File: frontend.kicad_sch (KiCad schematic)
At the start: 68 parts, among them P4 SMA, Q1 NMOS/PMOS, U12 BGS13SN8, U13 74LVC1G86, U14 BGS13SN8, U24 AP22652, U25 TRF37C73, U40 BGB741L7ESD

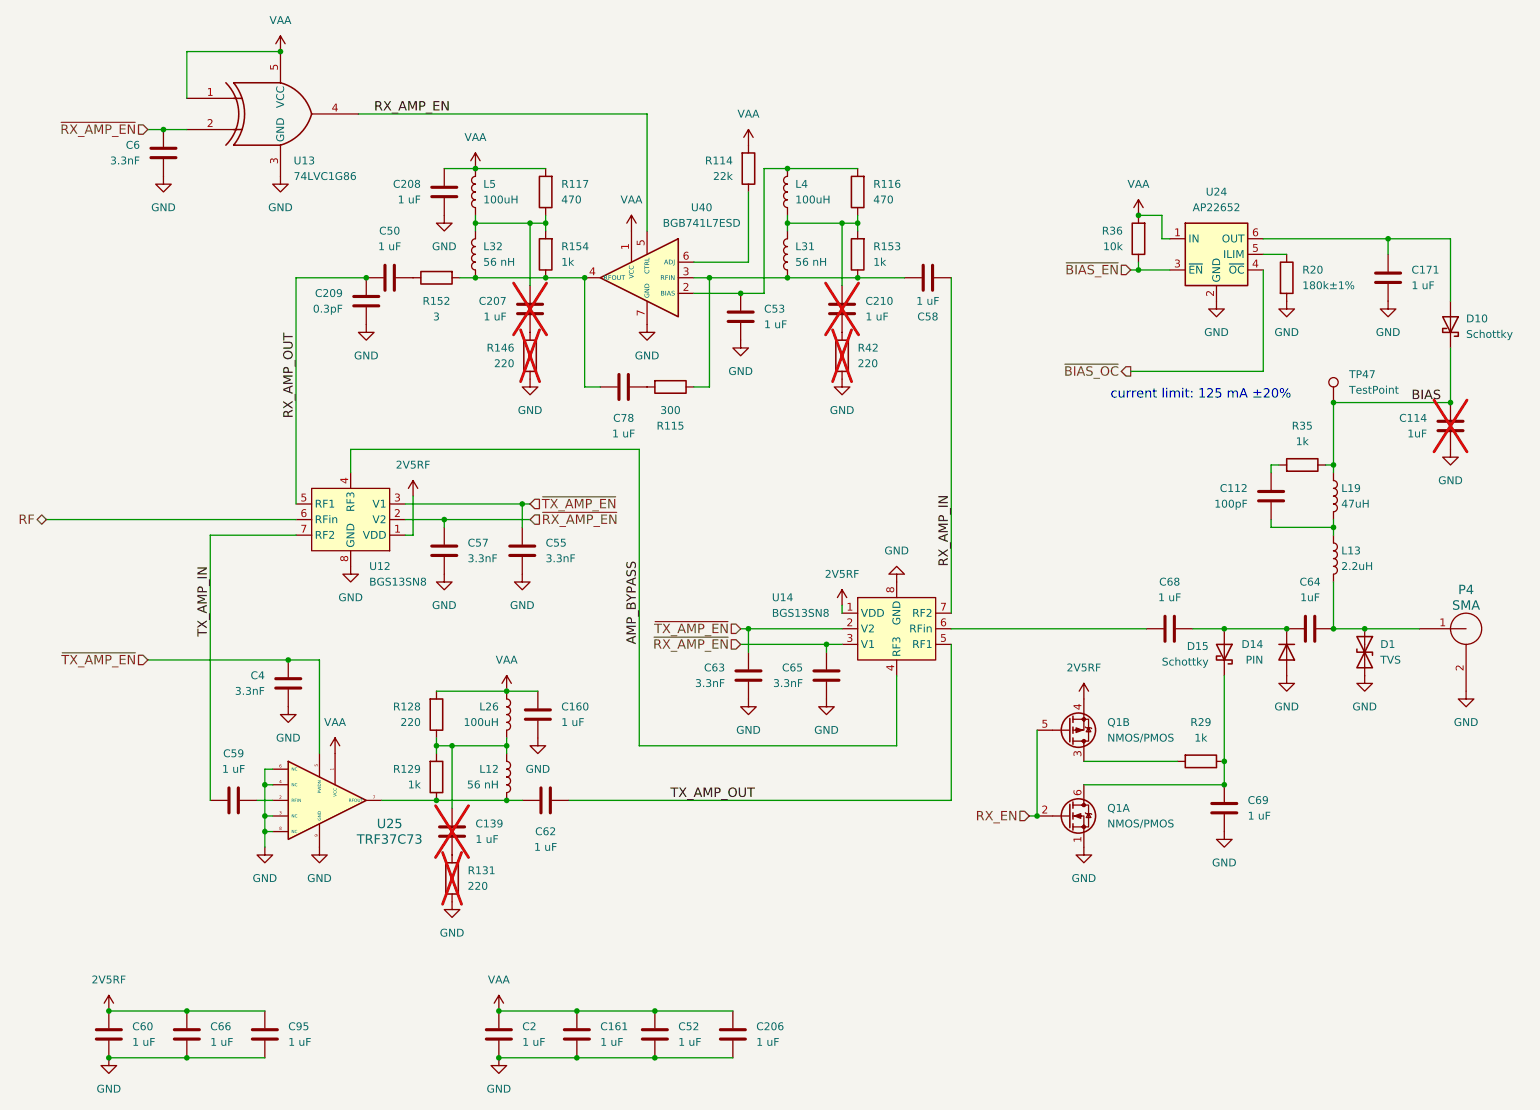
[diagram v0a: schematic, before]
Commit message: Standardize component Value fields
Use Tolerance field instead of expressing tolerance in Value field
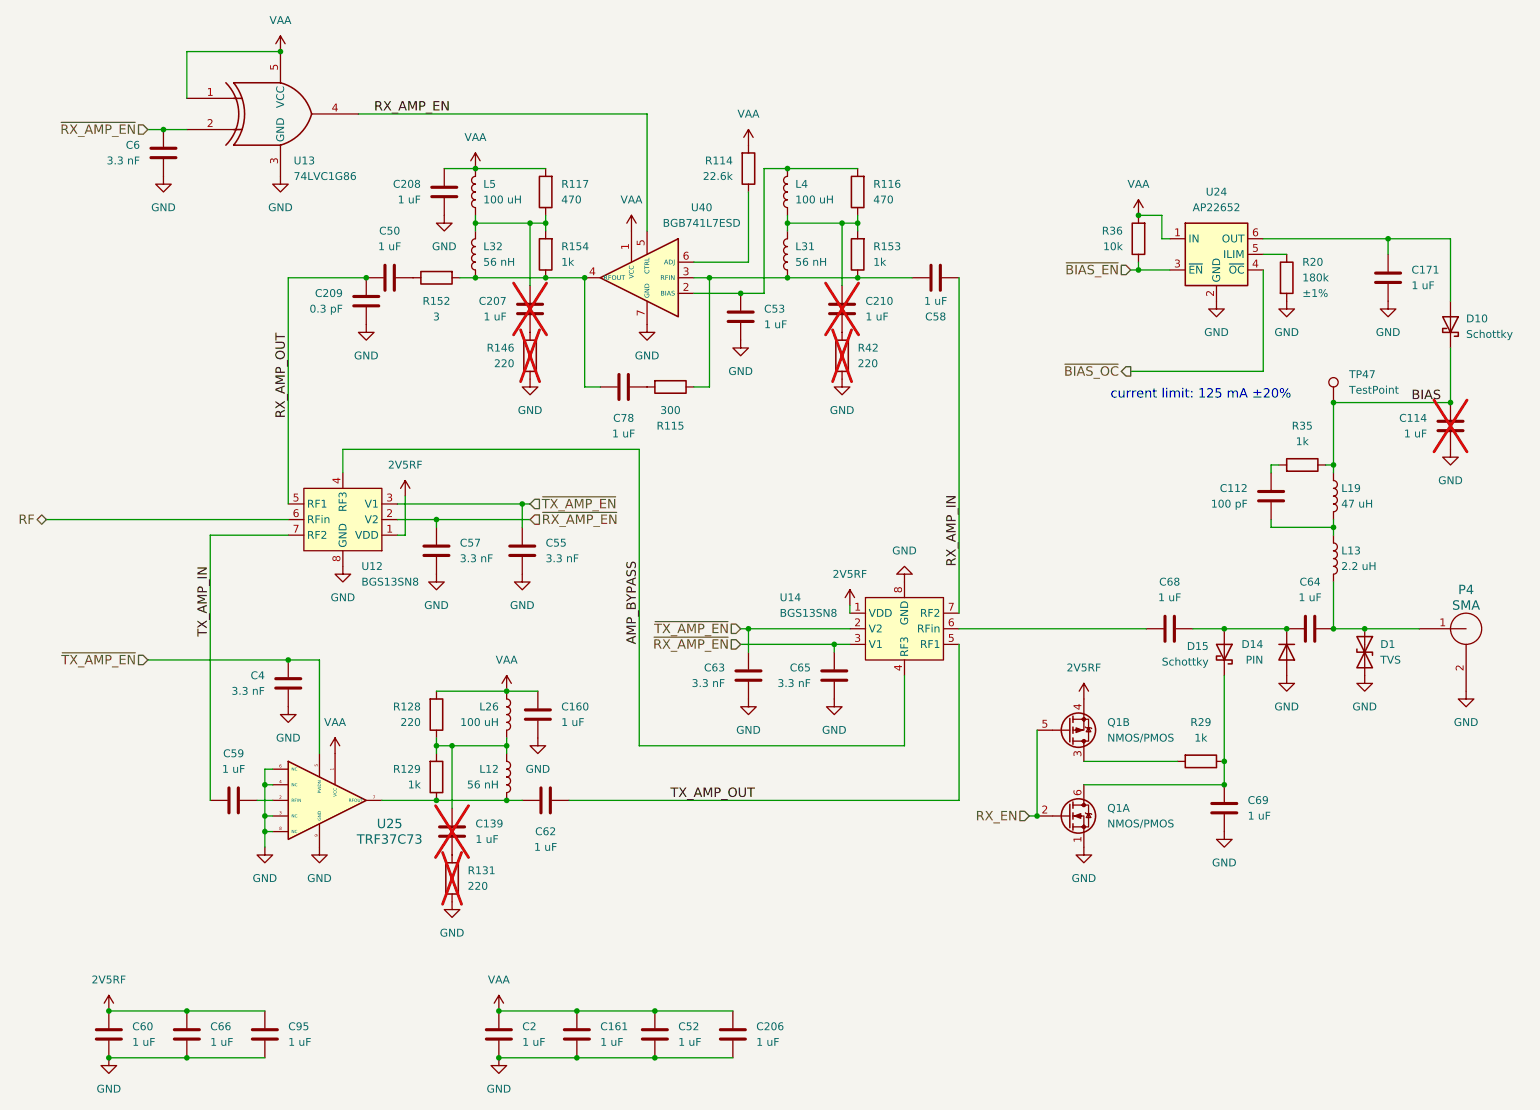
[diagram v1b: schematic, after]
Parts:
- C112: value 100pF -> 100 pF
- C114, C64: value 1uF -> 1 uF
- C209: value 0.3pF -> 0.3 pF
- C4, C55, C57, C6, C63, C65: value 3.3nF -> 3.3 nF
- L13: value 2.2uH -> 2.2 uH
- L19: value 47uH -> 47 uH
- L26, L4, L5: value 100uH -> 100 uH
- R114: value 22k -> 22.6k
- R20: value 180k±1% -> 180k; Tolerance (none) -> ±1%
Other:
- moved on the sheet: C57, C58, C65, U12, U14

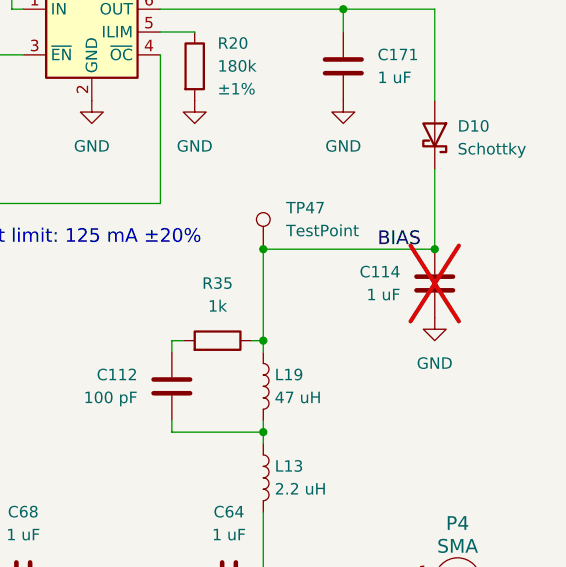
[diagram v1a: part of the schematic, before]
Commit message: Update U4 pull-ups
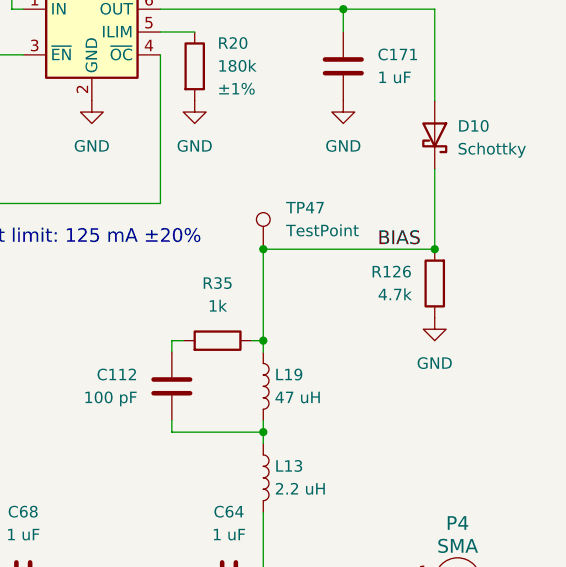
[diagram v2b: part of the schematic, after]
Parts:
- removed C114: 1 uF, Capacitor_SMD:C_0402_1005Metric, symbol Device:C
- added R126: 4.7k, Resistor_SMD:R_0201_0603Metric, symbol Device:R
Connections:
- net BIAS: now also R126.2
- net GND: now also R126.1
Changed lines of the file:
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@@
 	)
 	(junction
+		(at 265.43 78.74)
+		(diameter 0)
+		(color 0 0 0 0)
+	)
+	(junction
 		(at 214.63 57.15)
 		(diameter 0)
@@
 	)
 	(junction
-		(at 265.43 78.74)
-		(diameter 0)
-		(color 0 0 0 0)
-	)
-	(junction
 		(at 228.6 137.16)
 		(diameter 0)
@@
 	)
 	(symbol
-		(lib_id "Device:C")
-		(at 265.43 82.55 0)
-		(mirror x)
-		(unit 1)
-		(exclude_from_sim no)
-		(in_bom yes)
-		(on_board yes)
-		(dnp yes)
-		(fields_autoplaced yes)
-		(property "Reference" "C114"
-			(at 261.62 81.2799 0)
-			(effects
-				(font
-					(size 1.27 1.27)
-				)
-				(justify right)
-			)
-		)
-		(property "Value" "1 uF"
-			(at 261.62 83.8199 0)
-			(effects
-				(font
-					(size 1.27 1.27)
-				)
-				(justify right)
-			)
-		)
-		(property "Footprint" "Capacitor_SMD:C_0402_1005Metric"
-			(at 265.43 82.55 0)
-			(effects
-				(font
-					(size 1.524 1.524)
-				)
-				(hide yes)
-			)
-		)
-		(property "Datasheet" "~"
-			(at 265.43 82.55 0)
-			(effects
-				(font
-					(size 1.524 1.524)
-				)
-				(hide yes)
-			)
-		)
-		(property "Description" "CAP CER 1UF 25V X5R 0402"
-			(at 81.28 121.92 0)
-			(effects
-				(font
-					(size 1.524 1.524)
-				)
-				(hide yes)
-			)
-		)
-		(property "Manufacturer" "Samsung"
-			(at 81.28 121.92 0)
-			(effects
-				(font
-					(size 1.524 1.524)
-				)
-				(hide yes)
-			)
-		)
-		(property "Part Number" "CL05A105KA5NQNC"
-			(at 81.28 121.92 0)
-			(effects
-				(font
-					(size 1.524 1.524)
-				)
-				(hide yes)
-			)
-		)
-		(property "Substitution" "Murata GRM155R61E105KA12D"
-			(at 265.43 82.55 0)
-			(effects
-				(font
-					(size 1.27 1.27)
-				)
-				(hide yes)
-			)
-		)
-		(pin "1"
-		)
-		(pin "2"
-		)
-		(instances
-			(project "praline"
-				(path "/dba4afc6-760f-46cb-a936-032b76448f03/00000000-0000-0000-0000-0000503bb638"
-					(reference "C114")
-					(unit 1)
-				)
-			)
-		)
-	)
-	(symbol
 		(lib_id "Device:L")
 		(at 106.68 44.45 0)
@@
 					(unit 1)
 				)
+			)
+		)
+	)
+	(symbol
+		(lib_id "Device:R")
+		(at 265.43 82.55 180)
+		(unit 1)
+		(exclude_from_sim no)
+		(in_bom yes)
+		(on_board yes)
+		(dnp no)
+		(fields_autoplaced yes)
+		(property "Reference" "R126"
+			(at 262.89 81.2799 0)
+			(effects
+				(font
+					(size 1.27 1.27)
+				)
+				(justify left)
+			)
+		)
+		(property "Value" "4.7k"
+			(at 262.89 83.8199 0)
+			(effects
+				(font
+					(size 1.27 1.27)
+				)
+				(justify left)
+			)
+		)
+		(property "Footprint" "Resistor_SMD:R_0201_0603Metric"
+			(at 265.43 82.55 0)
+			(effects
+				(font
+					(size 1.524 1.524)
+				)
+				(hide yes)
+			)
+		)
+		(property "Datasheet" "~"
+			(at 265.43 82.55 0)
+			(effects
+				(font
+					(size 1.524 1.524)
+				)
+				(hide yes)
+			)
+		)
+		(property "Description" "RES 4.7K OHM 1% 1/20W 0201"
+			(at 265.43 82.55 0)
+			(effects
+				(font
+					(size 1.524 1.524)
+				)
+				(hide yes)
+			)
+		)
+		(property "Manufacturer" "Yageo"
+			(at 265.43 82.55 0)
+			(effects
+				(font
+					(size 1.524 1.524)
+				)
+				(hide yes)
+			)
+		)
+		(property "Part Number" "RC0201FR-074K7L"
+			(at 265.43 82.55 0)
+			(effects
+				(font
+					(size 1.524 1.524)
+				)
+				(hide yes)
+			)
+		)
+		(property "Substitution" "any equivalent"
+			(at 265.43 82.55 0)
+			(effects
+				(font
+					(size 1.27 1.27)
+				)
+				(hide yes)
+			)
+		)
+		(pin "1"
+		)
+		(pin "2"
+		)
+		(instances
+			(project "praline"
+				(path "/dba4afc6-760f-46cb-a936-032b76448f03/00000000-0000-0000-0000-0000503bb638"
+					(reference "R126")
+					(unit 1)
+				)

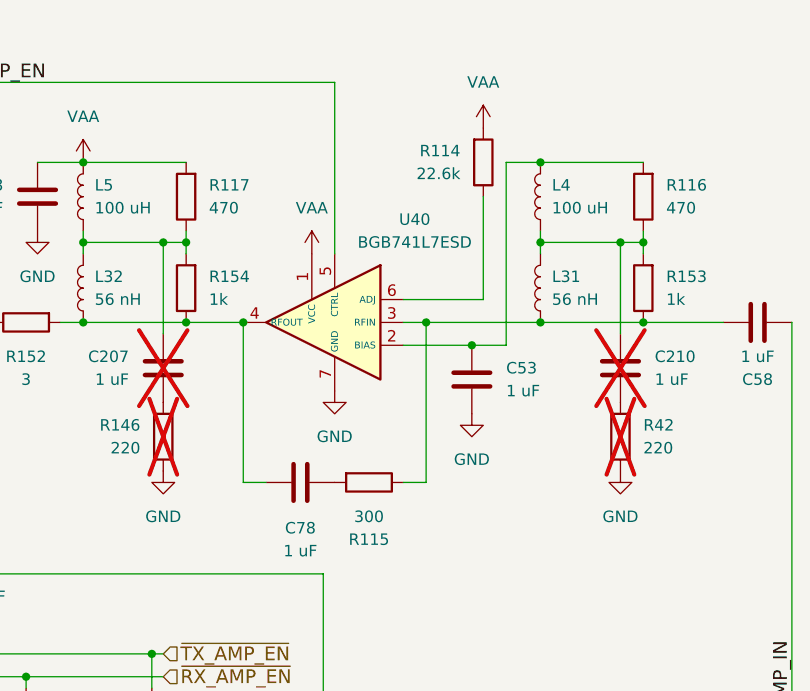
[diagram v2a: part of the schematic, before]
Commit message: Tune RX RF amp
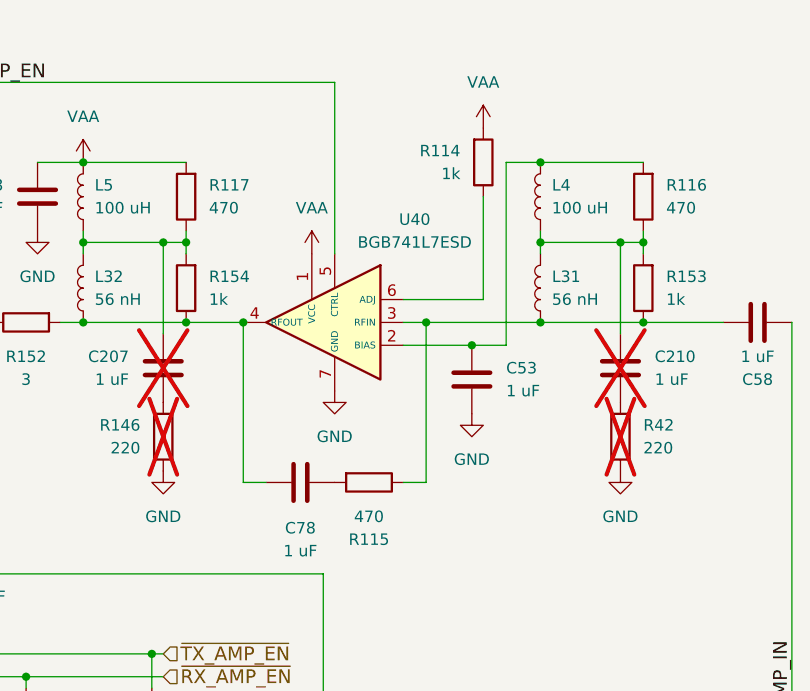
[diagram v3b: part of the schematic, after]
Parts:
- R114: value 22.6k -> 1k; Part Number RC0201FR-0722K6L -> RC0201FR-071KL
- R115: value 300 -> 470; Part Number RC0201FR-07300RL -> RC0201JR-07470RL
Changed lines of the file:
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@@
 			)
 		)
-		(property "Value" "22.6k"
+		(property "Value" "1k"
 			(at 148.59 41.9099 0)
 			(effects
@@
 			)
 		)
-		(property "Description" "RES 22.6K OHM 1% 1/20W 0201"
+		(property "Description" "RES 1K OHM 1% 1/20W 0201"
 			(at 151.13 40.64 0)
 			(effects
@@
 			)
 		)
-		(property "Part Number" "RC0201FR-0722K6L"
+		(property "Part Number" "RC0201FR-071KL"
 			(at 151.13 40.64 0)
 			(effects
@@
 			)
 		)
-		(property "Value" "300"
+		(property "Value" "470"
 			(at 138.43 80.01 90)
 			(effects
@@
 			)
 		)
-		(property "Description" "RES 300 OHM 1% 1/20W 0201"
+		(property "Description" "RES 470 OHM 5% 1/20W 0201"
 			(at 138.43 76.2 0)
 			(effects
@@
 			)
 		)
-		(property "Part Number" "RC0201FR-07300RL"
+		(property "Part Number" "RC0201JR-07470RL"
 			(at 138.43 76.2 90)
 			(effects

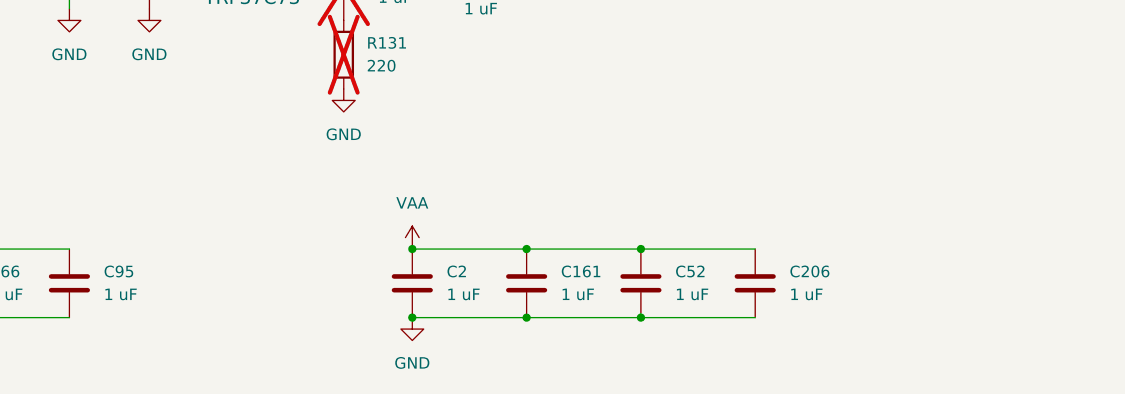
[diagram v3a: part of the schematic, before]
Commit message: Add more VAA, 1V2FPGA capacitance
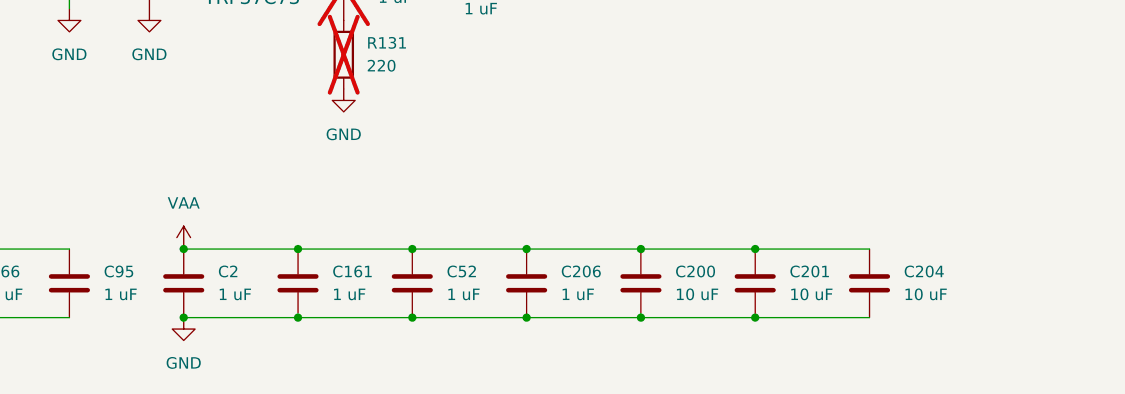
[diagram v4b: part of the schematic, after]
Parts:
- added C200, C201, C204: 10 uF, Capacitor_SMD:C_0805_2012Metric, symbol Device:C
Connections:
- net GND: now also C200.2, C201.2, C204.2
- net VAA: now also C200.1, C201.1, C204.1
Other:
- moved on the sheet: C161, C2, C206, C52

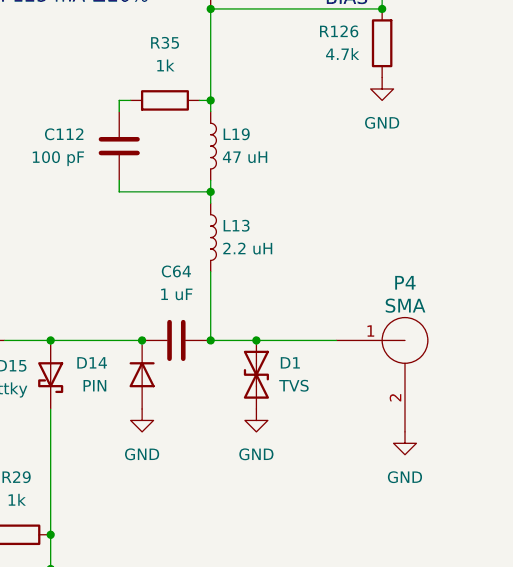
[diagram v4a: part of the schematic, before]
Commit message: Move mounting hole H7
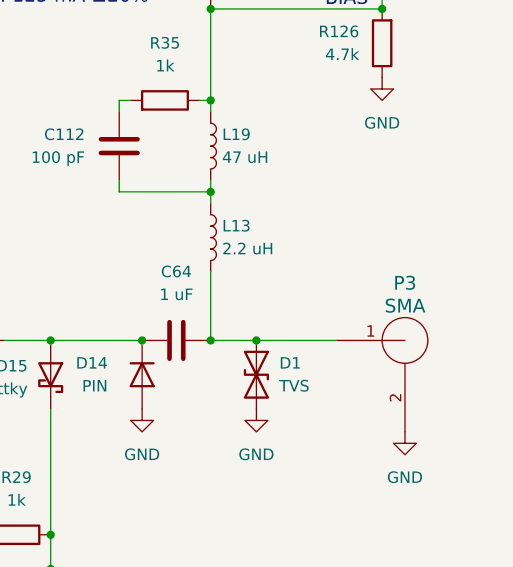
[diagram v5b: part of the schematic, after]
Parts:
- renumbered P4 to P3
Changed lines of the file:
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@@
 		(on_board yes)
 		(dnp no)
-		(property "Reference" "P4"
+		(property "Reference" "P3"
 			(at 267.97 109.22 0)
 			(effects
@@
 			(project ""
 				(path "/dba4afc6-760f-46cb-a936-032b76448f03/00000000-0000-0000-0000-0000503bb638"
-					(reference "P4")
+					(reference "P3")
 					(unit 1)
 				)
